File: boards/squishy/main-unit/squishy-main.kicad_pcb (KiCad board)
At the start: 8 copper layers, 10 x 5.2 mm, 265 parts, among them J1 REFCLK, J2 TRIGGER, J3 USB_C_Receptacle, J4 SU SWD, J5 Jack-DC, J6 MEM2061-01-188-00-A, J7 SCSI PHY Mezz, Q1 NTMFS5C442NT1G, Q10 PFET, Q2 NX6008NBKR, Q3 NX6008NBKR, Q4 NX6008NBKR, Q5 NX6008NBKR, Q6 PMPB20EN, Q8 DMN65D8L-7, Q9 DMN65D8L-7, SW1 RST, U1 LFE5UM5G-45F-8BG381C, U10 FUSB302BMPX, U11 ATSAMD09D14A-M, U12 GD25Q64EWIGR, U13 LM51551DSSR, U14 HyperRAM, U15 HyperRAM, U16 TPS7A1112PDRVT, U17 TPS7A1125PDRVT, U18 TPS73733DRVR, U19 INAx180, U2 HyperRAM, U20 TPS7A1112PDRVT, U21 AP3428/A, U3 HyperRAM, U4 APX811-40UG-7, U5 HD3SS460, U6 TPD4E02B04DQA, U7 SP3400-02UTG, U8 TPD4E02B04DQA, U9 USB3318, X1 100MHz, X2 13MHz, X3 200MHz, X4 48MHz

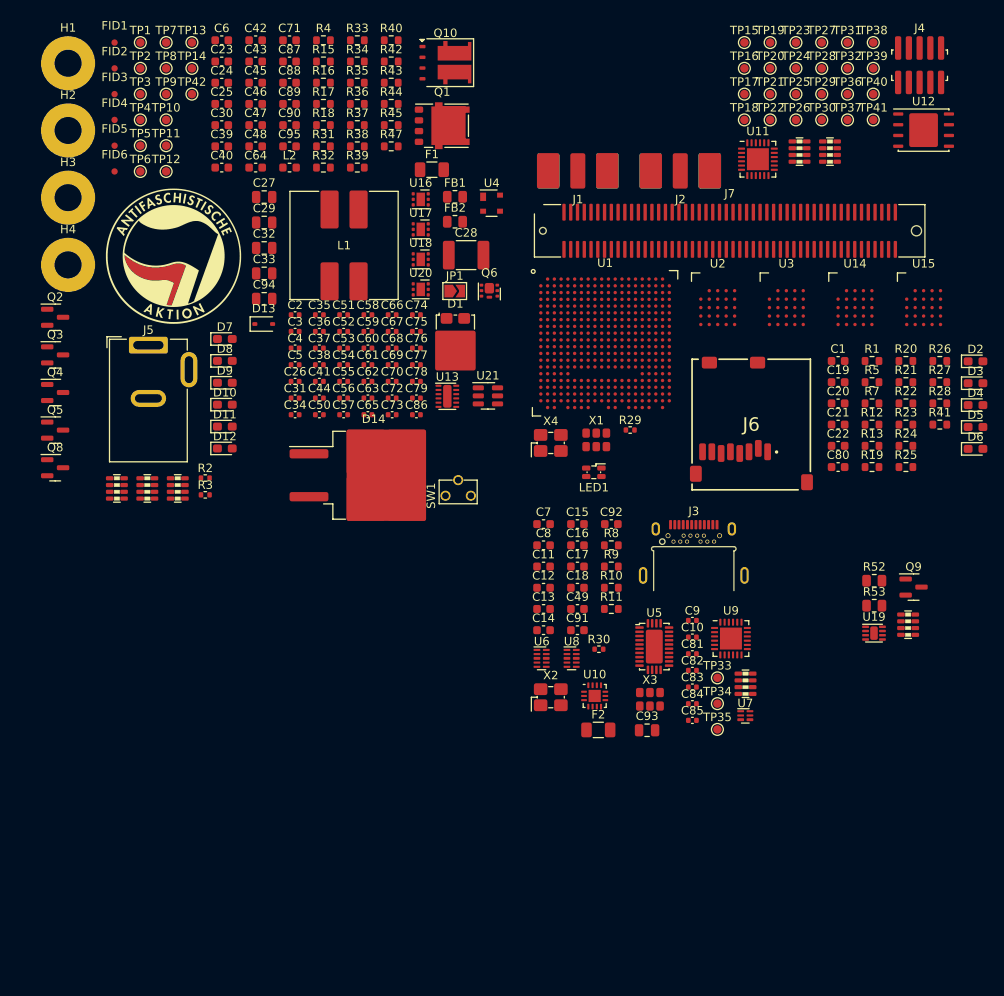
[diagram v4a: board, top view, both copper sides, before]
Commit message: squishy: main: Rough initial connection for the HyperRAM
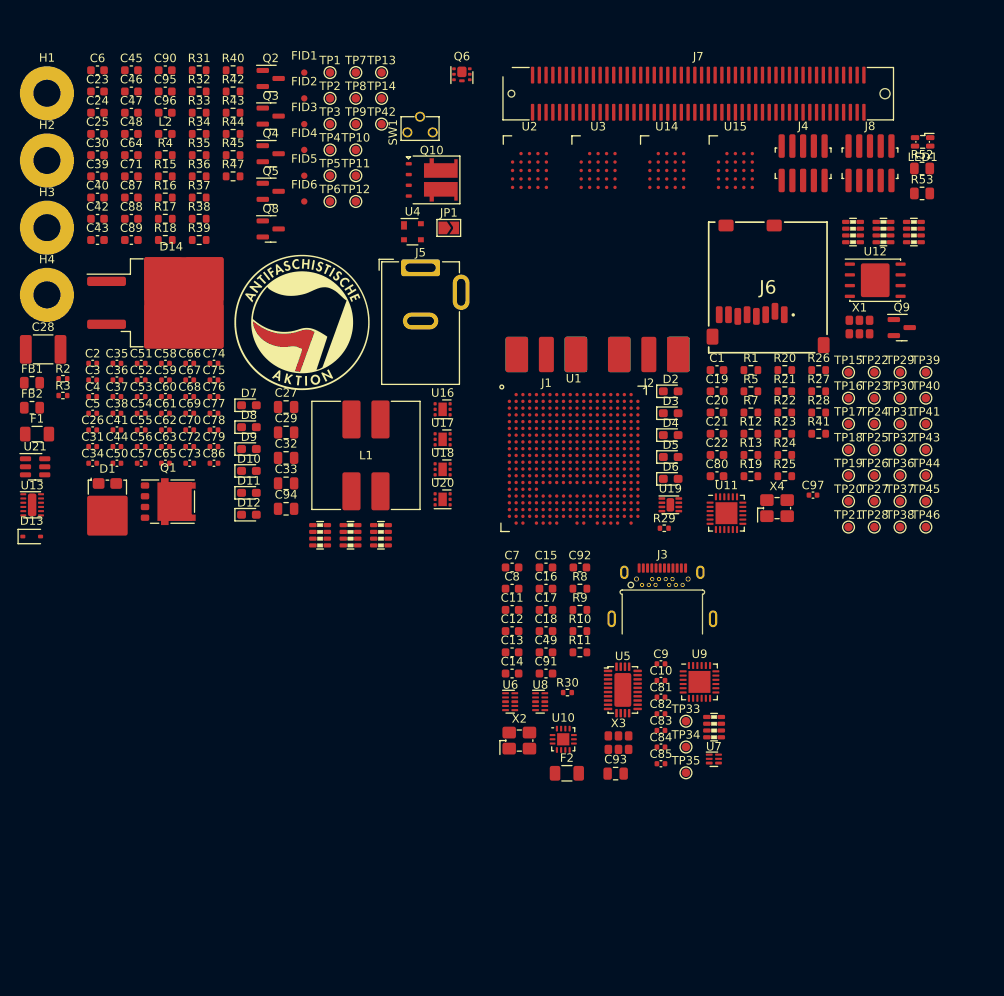
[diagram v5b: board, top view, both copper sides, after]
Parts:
- added C96: 100n, Capacitor_SMD:C_0603_1608Metric, F.Cu at (185.3, 27.2)
- added C97: 100n, Capacitor_SMD:C_0402_1005Metric, F.Cu at (261.9, 72.5)
- added J8: FLASH, lethalbit-connectors:FTSH-105-01-L-DV-K-TR, F.Cu at (268.6, 33.2)
- added TP43: ~{PHY_PWR_EN}, TestPoint:TestPoint_Pad_D1.0mm, F.Cu at (275.2, 67.1)
- added TP44: PHY_5v0, TestPoint:TestPoint_Pad_D1.0mm, F.Cu at (275.2, 70.2)
- added TP45: PHY_3v3, TestPoint:TestPoint_Pad_D1.0mm, F.Cu at (275.2, 73.2)
- added TP46: ~{SU_RST}, TestPoint:TestPoint_Pad_D1.0mm, F.Cu at (275.2, 76.2)
- U19: value INAx180 -> INA2180A3
- moved TP38 57.4 mm to (272.2, 76.2)
- moved F1 56.2 mm to (170.1, 65.2)
- moved LED1 55.1 mm to (274.9, 30.7)
- moved Q1 55.0 mm to (185.6, 73.2)
- moved FB1 54.7 mm to (169.5, 59.2)
- moved FB2 54.7 mm to (169.5, 62.1)
- moved TP27 54.6 mm to (269.1, 73.2)
- moved TP28 54.6 mm to (269.1, 76.2)
- moved U21 54.2 mm to (169.9, 69.1)
- moved TP19 52.1 mm to (266.1, 70.2)
- moved TP20 52.1 mm to (266.1, 73.2)
- moved TP21 52.1 mm to (266.1, 76.2)
- moved C28 51.3 mm to (170.8, 55.2)
- moved U13 50.8 mm to (169.5, 73.6)
- moved R52 49.1 mm to (274.8, 33.8)
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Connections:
- net Net-(J7-Pin_1) renamed /PHY_3v3
- net Net-(J7-Pin_2) renamed /PHY_5v0
- J1 pad 1: /CLKOUT -> Net-(J1-In)
- U1 pad C18: unconnected-(U1D-PR11A-PadC18) -> /RAM.~{CS0}
- U1 pad C20: unconnected-(U1D-PR23A-PadC20) -> /RAM.DQE0
- U1 pad D18: unconnected-(U1D-PR14A-PadD18) -> /RAM.~{CS1}
- U1 pad D19: unconnected-(U1D-PR23B-PadD19) -> /RAM.DQE1
- U1 pad D20: unconnected-(U1D-PR23C-PadD20) -> /RAM.DQE2
- U1 pad E18: unconnected-(U1D-PR14C-PadE18) -> /RAM.~{CS2}
- U1 pad E19: unconnected-(U1D-PR23D-PadE19) -> /RAM.DQE3
- U1 pad E20: unconnected-(U1D-PR26A-PadE20) -> /RAM.DQE4
- U1 pad F18: unconnected-(U1D-PR14D-PadF18) -> /RAM.~{CS3}
- U1 pad F19: unconnected-(U1D-PR26B-PadF19) -> /RAM.DQE5
- U1 pad F20: unconnected-(U1D-PR26C-PadF20) -> /RAM.DQE6
- U1 pad G18: unconnected-(U1D-PR17B-PadG18) -> /RAM.~{RST}
- U1 pad G19: unconnected-(U1D-PR29A-PadG19) -> /RAM.DQO0
- U1 pad G20: unconnected-(U1D-PR26D-PadG20) -> /RAM.DQE7
- U1 pad H18: unconnected-(U1D-PR20A-PadH18) -> /RAM.RWDS
- U1 pad H20: unconnected-(U1D-PR29B-PadH20) -> /RAM.DQO1
- U1 pad J18: unconnected-(U1D-PR29C-PadJ18) -> /RAM.DQO2
- U1 pad J19: unconnected-(U1D-PR32A-PadJ19) -> /RAM.DQO4
- U1 pad J20: unconnected-(U1D-PR32C-PadJ20) -> /RAM.DQO6
- U1 pad K18: unconnected-(U1D-PR29D-PadK18) -> /RAM.DQO3
- U1 pad K19: unconnected-(U1D-PR32B-PadK19) -> /RAM.DQO5
- U1 pad K20: unconnected-(U1D-PR32D-PadK20) -> /RAM.DQO7
- U1 pad R2: unconnected-(U1H-PB15A/HOLDN/DI/BUSY/~{CSSPI}/~{CE}-PadR2) -> /~{FPGA_HOLD}
- U11 pad 9: /SU_LED_1 -> /~{FPGA_HOLD}
- U19 pad 4: (no net) -> GND
- U19 pad 8: (no net) -> +3V3
- U19 pad 9: (no net) -> GND

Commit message: squishy: main: Rough initial connection for SD card
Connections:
- U1 pad L1: unconnected-(U1F-PL65C-PadL1) -> /SDCARD.D1
- U1 pad L2: unconnected-(U1F-PL62D-PadL2) -> /SDCARD.CMD
- U1 pad L3: unconnected-(U1F-PL62C-PadL3) -> /SDCARD.D3
- U1 pad M1: unconnected-(U1F-PL65B-PadM1) -> /SDCARD.DET
- U1 pad M3: unconnected-(U1F-PL62B-PadM3) -> /SDCARD.D2
- U1 pad N1: unconnected-(U1F-PL65D-PadN1) -> /SDCARD.D0
- U1 pad N2: unconnected-(U1F-PL65A-PadN2) -> /SDCARD.CLK

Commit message: squishy: main: rough initial connections for the ULPI PHY
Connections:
- U1 pad L20: unconnected-(U1E-PR35A-PadL20) -> /USB Frontend/PHY_BUS.CLK
- U1 pad M20: unconnected-(U1E-PR35B-PadM20) -> /USB Frontend/~{PHY_RST}
- U1 pad N19: unconnected-(U1E-PR59A-PadN19) -> /USB Frontend/PHY_BUS.NXT
- U1 pad N20: unconnected-(U1E-PR59B-PadN20) -> /USB Frontend/PHY_BUS.DIR
- U1 pad P18: unconnected-(U1E-PR59D-PadP18) -> /USB Frontend/PHY_BUS.D0
- U1 pad P19: unconnected-(U1E-PR59C-PadP19) -> /USB Frontend/PHY_BUS.STP
- U1 pad P20: unconnected-(U1E-PR62A-PadP20) -> /USB Frontend/PHY_BUS.D1
- U1 pad R18: unconnected-(U1E-PR65B-PadR18) -> /USB Frontend/PHY_BUS.D6
- U1 pad R20: unconnected-(U1E-PR62B-PadR20) -> /USB Frontend/PHY_BUS.D2
- U1 pad T19: unconnected-(U1E-PR65A-PadT19) -> /USB Frontend/PHY_BUS.D5
- U1 pad T20: unconnected-(U1E-PR62C-PadT20) -> /USB Frontend/PHY_BUS.D3
- U1 pad U19: unconnected-(U1E-PR65C-PadU19) -> /USB Frontend/PHY_BUS.D7
- U1 pad U20: unconnected-(U1E-PR62D-PadU20) -> /USB Frontend/PHY_BUS.D4

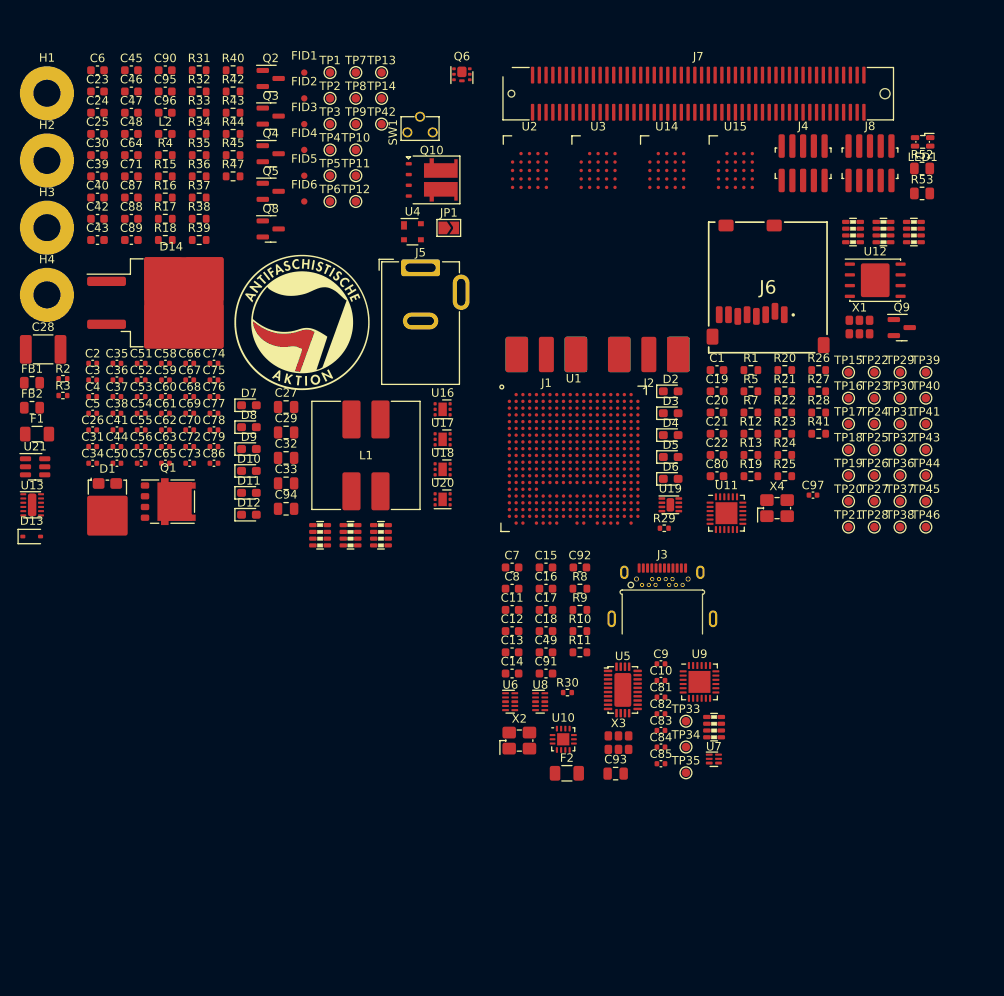
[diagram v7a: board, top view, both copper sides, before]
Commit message: squishy: main: Some final cleanup, made ERC clean, hooked up some more rough ordering for IO pins for the SCSI PHY, Replaced the 3v3 LDO with a buck due to other rails hanging off of it.
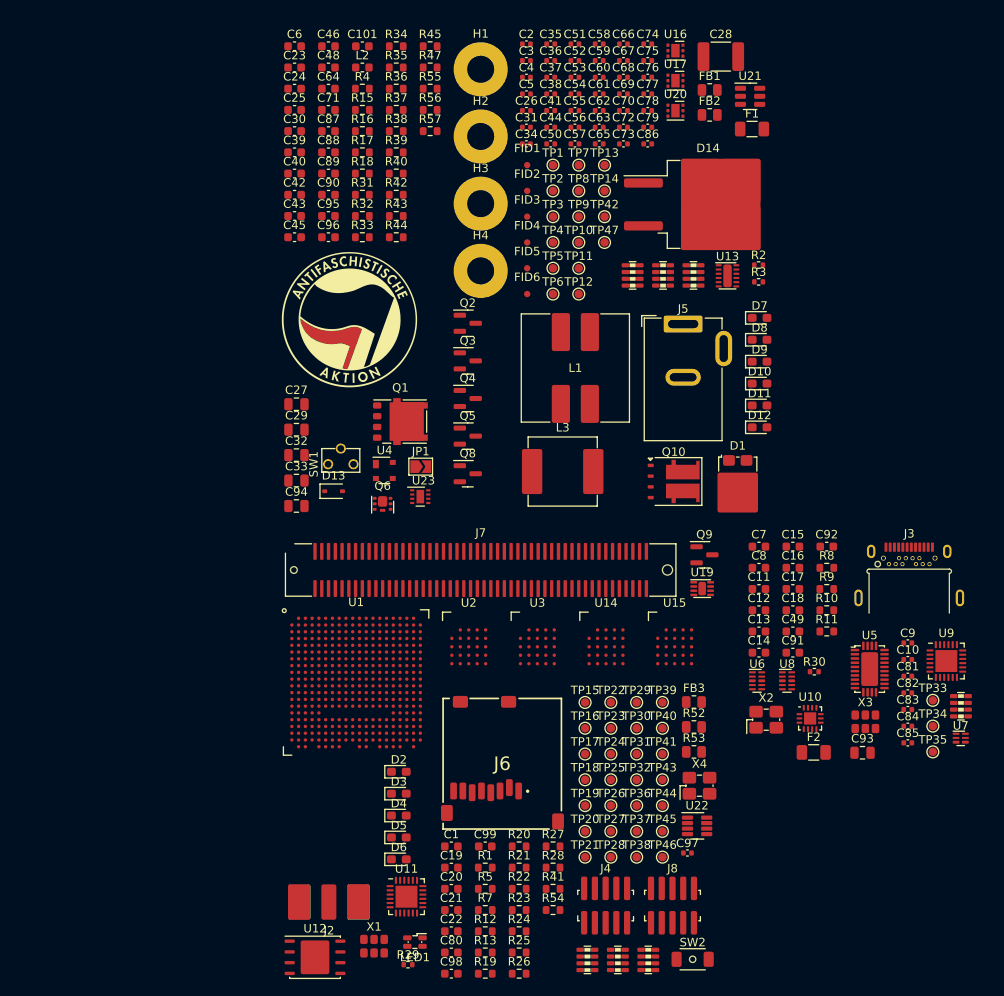
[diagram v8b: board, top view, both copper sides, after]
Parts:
- removed C47: 1u, Capacitor_SMD:C_0603_1608Metric
- removed J1: REFCLK, lethalbit-rf:Molex_SMA_732512120
- removed U18: TPS73733DRVR, Package_SON:WSON-6-1EP_2x2mm_P0.65mm_EP1x1.6mm
- added C101: 22u, Capacitor_SMD:C_0603_1608Metric, F.Cu at (208.6, 19.4)
- added C98: 100n, Capacitor_SMD:C_0603_1608Metric, F.Cu at (219.1, 129.1)
- added C99: 1u, Capacitor_SMD:C_0603_1608Metric, F.Cu at (223.1, 114.0)
- added FB3: 600 @ 100MHz, Resistor_SMD:R_0805_2012Metric, F.Cu at (247.8, 97.0)
- added L3: 1u, lethalbit-inductor:L_Vishay_IHLP-3232, F.Cu at (232.3, 69.7)
- added R54: 10k, Resistor_SMD:R_0603_1608Metric, F.Cu at (231.1, 121.6)
- added R55: 249k, Resistor_SMD:R_0603_1608Metric, F.Cu at (216.6, 24.4)
- added R56: 39k2, Resistor_SMD:R_0603_1608Metric, F.Cu at (216.6, 26.9)
- added R57: 178k, Resistor_SMD:R_0603_1608Metric, F.Cu at (216.6, 29.4)
- added SW2: DFU, rhais_button-smd:B3U-1000P-B, F.Cu at (247.7, 127.4)
- added TP47: SEPIC_GOOD, TestPoint:TestPoint_Pad_D1.0mm, F.Cu at (237.2, 42.6)
- added U22: MAX1118, Package_TO_SOT_SMD:SOT-23-8, F.Cu at (248.2, 111.6)
- added U23: TLV62084ADSGx, Package_SON:WSON-8-1EP_2x2mm_P0.5mm_EP0.9x1.6mm, F.Cu at (215.4, 72.7)
- C46: value 1u -> 10u
- R52, R53: value 100m -> 50m
- U19: value INA2180A3 -> INA2180A1
- moved LED1 112.1 mm to (214.8, 125.3)
- moved U12 104.0 mm to (203.0, 127.2)
- moved U21 95.3 mm to (254.5, 25.3)
- moved X1 93.1 mm to (210.0, 125.8)
- moved F1 92.0 mm to (254.7, 29.2)
- moved R14 91.7 mm to (238.8, 127.5)
- moved R51 91.7 mm to (242.4, 127.5)
- moved R6 91.7 mm to (235.2, 127.5)
- moved J4 90.9 mm to (237.4, 121.0)
- moved J8 90.9 mm to (245.3, 121.0)
- moved C28 87.3 mm to (251.0, 20.6)
- moved FB1 87.3 mm to (249.7, 24.5)
- moved FB2 87.3 mm to (249.7, 27.5)
- moved U13 86.6 mm to (251.8, 46.5)
- moved R2 83.4 mm to (255.5, 45.2)
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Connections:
- C42 pad 1: +1V2 -> +1V2A
- C88 pad 1: +3V3 -> +5V
- C97 pad 1: Net-(J1-In) -> /ADC_REF
- C97 pad 2: /CLKOUT -> GND
- J7 pad 11: unconnected-(J7-Pin_11-Pad11) -> /ID_SCL
- J7 pad 12: unconnected-(J7-Pin_12-Pad12) -> /SCSI_PHY.IO
- J7 pad 13: unconnected-(J7-Pin_13-Pad13) -> /ID_SDA
- J7 pad 14: unconnected-(J7-Pin_14-Pad14) -> /SCSI_PHY.REQ
- J7 pad 17: unconnected-(J7-Pin_17-Pad17) -> /TERMPW_EN
- J7 pad 18: unconnected-(J7-Pin_18-Pad18) -> /SCSI_PHY.CD
- J7 pad 20: unconnected-(J7-Pin_20-Pad20) -> /SCSI_PHY.SEL
- J7 pad 24: unconnected-(J7-Pin_24-Pad24) -> /SCSI_PHY.MSG
- J7 pad 26: unconnected-(J7-Pin_26-Pad26) -> /SCSI_PHY.RST
- J7 pad 30: unconnected-(J7-Pin_30-Pad30) -> /SCSI_PHY.ACK
- J7 pad 32: unconnected-(J7-Pin_32-Pad32) -> /SCSI_PHY.BSY
- J7 pad 36: unconnected-(J7-Pin_36-Pad36) -> /SCSI_PHY.ATN
- J7 pad 38: unconnected-(J7-Pin_38-Pad38) -> /SCSI_PHY.SINDLE
- J7 pad 41: unconnected-(J7-Pin_41-Pad41) -> /SCSI_PHY.DB31
- J7 pad 42: unconnected-(J7-Pin_42-Pad42) -> /SCSI_PHY.RMT_START
- J7 pad 43: unconnected-(J7-Pin_43-Pad43) -> /SCSI_PHY.DB30
- J7 pad 44: unconnected-(J7-Pin_44-Pad44) -> /SCSI_PHY.DYLD_START
- J7 pad 47: unconnected-(J7-Pin_47-Pad47) -> /SCSI_PHY.DB29
- J7 pad 48: unconnected-(J7-Pin_48-Pad48) -> /SCSI_PHY.DP0/CRCA
- J7 pad 49: unconnected-(J7-Pin_49-Pad49) -> /SCSI_PHY.DB28
- J7 pad 50: unconnected-(J7-Pin_50-Pad50) -> /SCSI_PHY.DP1
- J7 pad 53: unconnected-(J7-Pin_53-Pad53) -> /SCSI_PHY.DB27
- J7 pad 54: unconnected-(J7-Pin_54-Pad54) -> /SCSI_PHY.ID0
- J7 pad 55: unconnected-(J7-Pin_55-Pad55) -> /SCSI_PHY.DB26
- J7 pad 56: unconnected-(J7-Pin_56-Pad56) -> /SCSI_PHY.ID1
- J7 pad 59: unconnected-(J7-Pin_59-Pad59) -> /SCSI_PHY.DB25
- J7 pad 60: unconnected-(J7-Pin_60-Pad60) -> /SCSI_PHY.ID2
- J7 pad 61: unconnected-(J7-Pin_61-Pad61) -> /SCSI_PHY.DB24
- J7 pad 62: unconnected-(J7-Pin_62-Pad62) -> /SCSI_PHY.ID3
- J7 pad 65: unconnected-(J7-Pin_65-Pad65) -> /SCSI_PHY.DB23
- J7 pad 66: unconnected-(J7-Pin_66-Pad66) -> /SCSI_PHY.DB0
- J7 pad 67: unconnected-(J7-Pin_67-Pad67) -> /SCSI_PHY.DB22
- J7 pad 68: unconnected-(J7-Pin_68-Pad68) -> /SCSI_PHY.DB1
- J7 pad 71: unconnected-(J7-Pin_71-Pad71) -> /SCSI_PHY.DB21
- J7 pad 72: unconnected-(J7-Pin_72-Pad72) -> /SCSI_PHY.DB2
- J7 pad 73: unconnected-(J7-Pin_73-Pad73) -> /SCSI_PHY.DB20
- J7 pad 74: unconnected-(J7-Pin_74-Pad74) -> /SCSI_PHY.DB3
- J7 pad 77: unconnected-(J7-Pin_77-Pad77) -> /SCSI_PHY.DB19
- J7 pad 78: unconnected-(J7-Pin_78-Pad78) -> /SCSI_PHY.DB4
- J7 pad 79: unconnected-(J7-Pin_79-Pad79) -> /SCSI_PHY.DB18
- J7 pad 80: unconnected-(J7-Pin_80-Pad80) -> /SCSI_PHY.DB5
- J7 pad 83: unconnected-(J7-Pin_83-Pad83) -> /SCSI_PHY.DB17
- J7 pad 84: unconnected-(J7-Pin_84-Pad84) -> /SCSI_PHY.DB6
- J7 pad 85: unconnected-(J7-Pin_85-Pad85) -> /SCSI_PHY.DB16
- J7 pad 86: unconnected-(J7-Pin_86-Pad86) -> /SCSI_PHY.DB7
- J7 pad 89: unconnected-(J7-Pin_89-Pad89) -> /SCSI_PHY.DB15
- J7 pad 90: unconnected-(J7-Pin_90-Pad90) -> /SCSI_PHY.DB8
- J7 pad 91: unconnected-(J7-Pin_91-Pad91) -> /SCSI_PHY.DB14
- J7 pad 92: unconnected-(J7-Pin_92-Pad92) -> /SCSI_PHY.DB9
- J7 pad 95: unconnected-(J7-Pin_95-Pad95) -> /SCSI_PHY.DB13
- J7 pad 96: unconnected-(J7-Pin_96-Pad96) -> /SCSI_PHY.DB10
- J7 pad 97: unconnected-(J7-Pin_97-Pad97) -> /SCSI_PHY.DB12
- J7 pad 98: unconnected-(J7-Pin_98-Pad98) -> /SCSI_PHY.DB11
- R45 pad 2: +1V2 -> +1V2A
- TP2 pad 1: +1V2 -> +1V2A
- U1 pad A10: unconnected-(U1B-PT36A-PadA10) -> /SCSI_PHY.DB10
- U1 pad A11: unconnected-(U1B-PT36B-PadA11) -> /SCSI_PHY.DB11
- U1 pad A12: unconnected-(U1C-PT49A-PadA12) -> /SCSI_PHY.ID2
- U1 pad A13: unconnected-(U1C-PT49B-PadA13) -> /SCSI_PHY.ID3
- U1 pad A14: unconnected-(U1C-PT56A-PadA14) -> /SCSI_PHY.DB29
- U1 pad A15: unconnected-(U1C-PT67A-PadA15) -> /SCSI_PHY.DB27
- U1 pad A16: unconnected-(U1C-PT74A-PadA16) -> /SCSI_PHY.DB16
- U1 pad A17: unconnected-(U1C-PT80A-PadA17) -> /SCSI_PHY.DB21
- U1 pad A18: unconnected-(U1C-PT83A-PadA18) -> /SCSI_PHY.DB23
- U1 pad A19: unconnected-(U1C-PT85A-PadA19) -> /SCSI_PHY.DB25
- U1 pad A2: unconnected-(U1G-PL23A-PadA2) -> /SCSI_PHY.DB0
- U1 pad A3: unconnected-(U1G-PL14C-PadA3) -> /SCSI_PHY.SEL
- U1 pad A4: unconnected-(U1G-PL11A-PadA4) -> /ID_SCL
- U1 pad A5: unconnected-(U1G-PL11B-PadA5) -> /ID_SDA
- U1 pad A6: unconnected-(U1B-PT4A-PadA6) -> /SCSI_PHY.ACK
- U1 pad A7: unconnected-(U1B-PT18A-PadA7) -> /SCSI_PHY.DP0/CRCA
- U1 pad A8: unconnected-(U1B-PT18B-PadA8) -> /SCSI_PHY.DP1
- U1 pad A9: unconnected-(U1B-PT33A-PadA9) -> /SCSI_PHY.DB8
- U1 pad B1: unconnected-(U1G-PL23B-PadB1) -> /SCSI_PHY.DB1
- U1 pad B10: unconnected-(U1B-PT33B-PadB10) -> /SCSI_PHY.DB9
- U1 pad B11: unconnected-(U1B-PT38A-PadB11) -> /SCSI_PHY.DB12
- U1 pad B12: unconnected-(U1C-PT44A-PadB12) -> /SCSI_PHY.ID0
- U1 pad B13: unconnected-(U1C-PT51A-PadB13) -> /SCSI_PHY.DB31
- U1 pad B15: unconnected-(U1C-PT69A-PadB15) -> /SCSI_PHY.DB14
- U1 pad B16: unconnected-(U1C-PT74B-PadB16) -> /SCSI_PHY.DB17
- U1 pad B17: unconnected-(U1C-PT78A-PadB17) -> /SCSI_PHY.DB19
- U1 pad B18: unconnected-(U1C-PT80B-PadB18) -> /SCSI_PHY.DB22
- U1 pad B19: unconnected-(U1C-PT83B-PadB19) -> /SCSI_PHY.DB24
- U1 pad B2: unconnected-(U1G-PL23C-PadB2) -> /SCSI_PHY.DB2
- U1 pad B20: unconnected-(U1C-PT85B-PadB20) -> /SCSI_PHY.DB26
- U1 pad B3: unconnected-(U1G-PL14D-PadB3) -> /SCSI_PHY.MSG
- U1 pad B4: unconnected-(U1G-PL14B-PadB4) -> /SCSI_PHY.CD
- U1 pad B5: unconnected-(U1G-PL11C-PadB5) -> /TERMPW_EN
- U1 pad B6: unconnected-(U1B-PT4B-PadB6) -> /SCSI_PHY.BSY
- U1 pad B8: unconnected-(U1B-PT15B-PadB8) -> /SCSI_PHY.DYLD_START
- U1 pad B9: unconnected-(U1B-PT31A-PadB9) -> /SCSI_PHY.DB6
- U1 pad C1: unconnected-(U1G-PL26A-PadC1) -> /SCSI_PHY.DB4
- U1 pad C10: unconnected-(U1B-PT31B-PadC10) -> /SCSI_PHY.DB7
- U1 pad C11: unconnected-(U1B-PT38B-PadC11) -> /SCSI_PHY.DB13
- U1 pad C12: unconnected-(U1C-PT44B-PadC12) -> /SCSI_PHY.ID1
- U1 pad C13: unconnected-(U1C-PT51B-PadC13) -> /SCSI_PHY.DB30
- U1 pad C14: unconnected-(U1C-PT56B-PadC14) -> /SCSI_PHY.DB28
- U1 pad C15: unconnected-(U1C-PT69B-PadC15) -> /SCSI_PHY.DB15
- U1 pad C16: unconnected-(U1C-PT76A-PadC16) -> /SCSI_PHY.DB18
- U1 pad C17: unconnected-(U1C-PT78B-PadC17) -> /SCSI_PHY.DB20
- U1 pad C2: unconnected-(U1G-PL23D-PadC2) -> /SCSI_PHY.DB3
- U1 pad C3: unconnected-(U1G-PL17C-PadC3) -> /SCSI_PHY.RST
- U1 pad C4: unconnected-(U1G-PL14A-PadC4) -> /SCSI_PHY.REQ
- U1 pad C5: unconnected-(U1G-PL11D-PadC5) -> /SCSI_PHY.IO
- U1 pad C6: unconnected-(U1B-PT11A-PadC6) -> /SCSI_PHY.ATN
- U1 pad C7: unconnected-(U1B-PT11B-PadC7) -> /SCSI_PHY.SINDLE
- U1 pad C8: unconnected-(U1B-PT15A-PadC8) -> /SCSI_PHY.RMT_START
- U1 pad C9: unconnected-(U1B-PT27A-PadC9) -> /SCSI_PHY.DB5
- U1 pad F1: unconnected-(U1F-PL35B-PadF1) -> /ADC_DAT
- U1 pad F10: Net-(U1A-VCCIO0-PadF10) -> +3V3
- U1 pad F11: Net-(U1A-VCCIO1-PadF11) -> +3V3
- U1 pad F12: Net-(U1A-VCCIO1-PadF11) -> +3V3
- U1 pad F9: Net-(U1A-VCCIO0-PadF10) -> +3V3
- U1 pad G2: unconnected-(U1F-PL35A-PadG2) -> /ADC_CLK
- U1 pad H1: unconnected-(U1F-PL41C-PadH1) -> /TRIGGER
- U1 pad H17: unconnected-(U1D-PR20B-PadH17) -> /RAM.DQO6
- U1 pad H2: unconnected-(U1F-PL35C-PadH2) -> /ADC_CH
- U1 pad H6: Net-(U1A-VCCIO7-PadH6) -> +3V3
- U1 pad H7: Net-(U1A-VCCIO7-PadH6) -> +3V3
- U1 pad J1: unconnected-(U1F-PL41B-PadJ1) -> /SU_ATTN
- U1 pad J17: unconnected-(U1D-PR20C-PadJ17) -> /RAM.DQO7
- U1 pad J20: /RAM.DQO6 -> /RAM.CLK
- U1 pad J6: Net-(U1A-VCCIO7-PadH6) -> +3V3
- U1 pad K1: unconnected-(U1F-PL41D-PadK1) -> /~{DFU_TRIG}
- U1 pad K20: /RAM.DQO7 -> /RAM.~{CLK}
- U1 pad K4: unconnected-(U1F-PL44A-PadK4) -> /FPGA_LED5
- U1 pad K5: unconnected-(U1F-PL44B-PadK5) -> /FPGA_LED4
- U1 pad L18: unconnected-(U1E-PR38C-PadL18) -> /USB Frontend/PD_SCL
- U1 pad L4: unconnected-(U1F-PL44C-PadL4) -> /FPGA_LED3
- U1 pad L5: unconnected-(U1F-PL44D-PadL5) -> /FPGA_LED2
- U1 pad M18: unconnected-(U1E-PR38D-PadM18) -> /USB Frontend/PD_SCA
- U1 pad M19: unconnected-(U1E-PR35D-PadM19) -> /USB Frontend/PLUG_POL
- U1 pad M5: unconnected-(U1F-PL53A-PadM5) -> /FPGA_LED1
- U1 pad N18: unconnected-(U1E-PR41C-PadN18) -> /USB Frontend/~{PD_INT}
- U1 pad T11: +1V2 -> +1V2A
- U1 pad T13: +1V2 -> +1V2A
- U1 pad T14: +1V2 -> +1V2A
- U1 pad T15: +1V2 -> +1V2A
- U1 pad T6: +1V2 -> +1V2A
- U1 pad U15: +1V2 -> +1V2A
- U1 pad U2: unconnected-(U1H-PB13B/~{CS1}-PadU2) -> /FPGA_CCLK
- U1 pad U6: +1V2 -> +1V2A
- U11 pad 8: /SU_LED_0 -> Net-(U11-PA09)
- U16 pad 1: +1V2 -> +1V2A
- U16 pad 2: +1V2 -> +1V2A
- U17 pad 3: +1V2 -> +1V2A
- U21 pad 3: +3V3 -> +5V
